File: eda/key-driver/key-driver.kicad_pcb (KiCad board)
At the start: 2 copper layers, 98.7 x 61.5 mm, 49 parts, among them J1 Conn_01x03_Socket, J10 Screw_Terminal_01x02, J11 Screw_Terminal_01x02, J12 Screw_Terminal_01x02, J13 Screw_Terminal_01x02, J14 Screw_Terminal_01x02, J15 Screw_Terminal_01x02, J2 Conn_01x03_Socket, J3 Screw_Terminal_01x02, J5 Screw_Terminal_01x02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

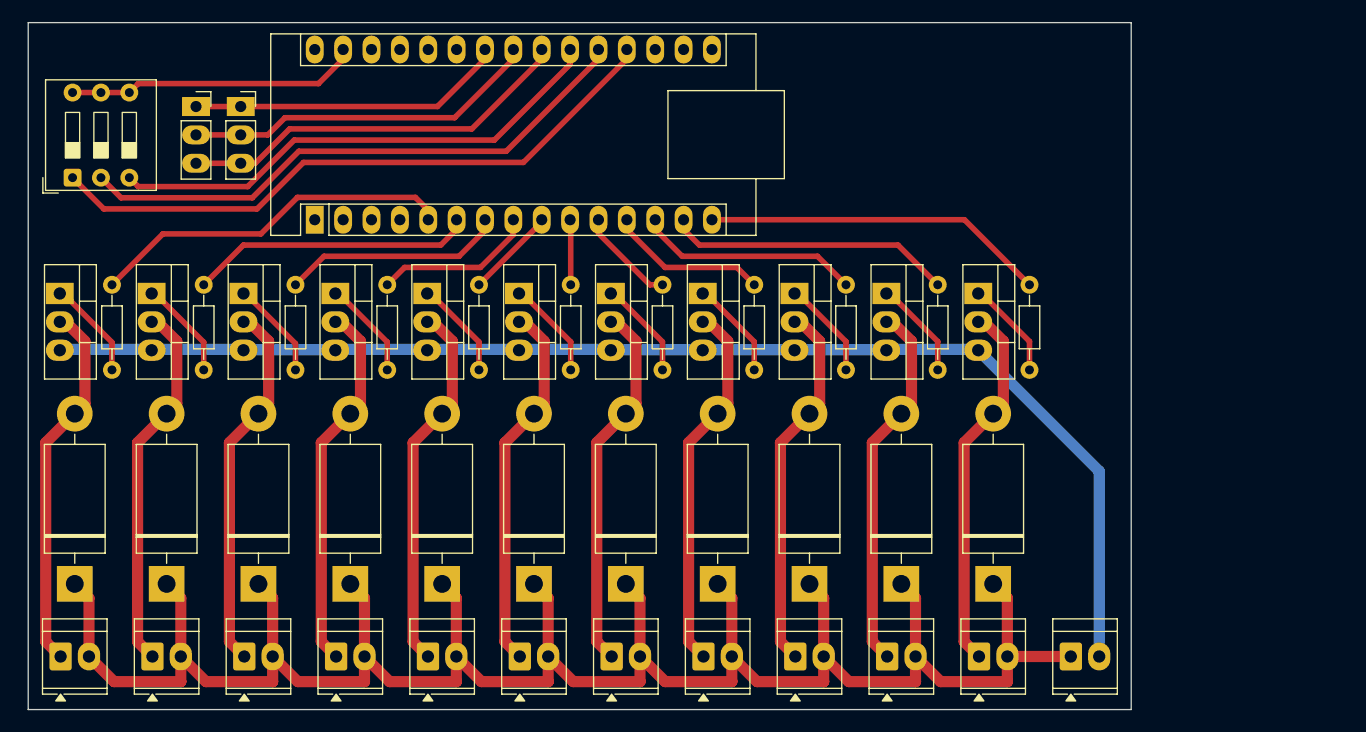
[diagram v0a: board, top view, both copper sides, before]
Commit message: Improve key driver circuit (r3)
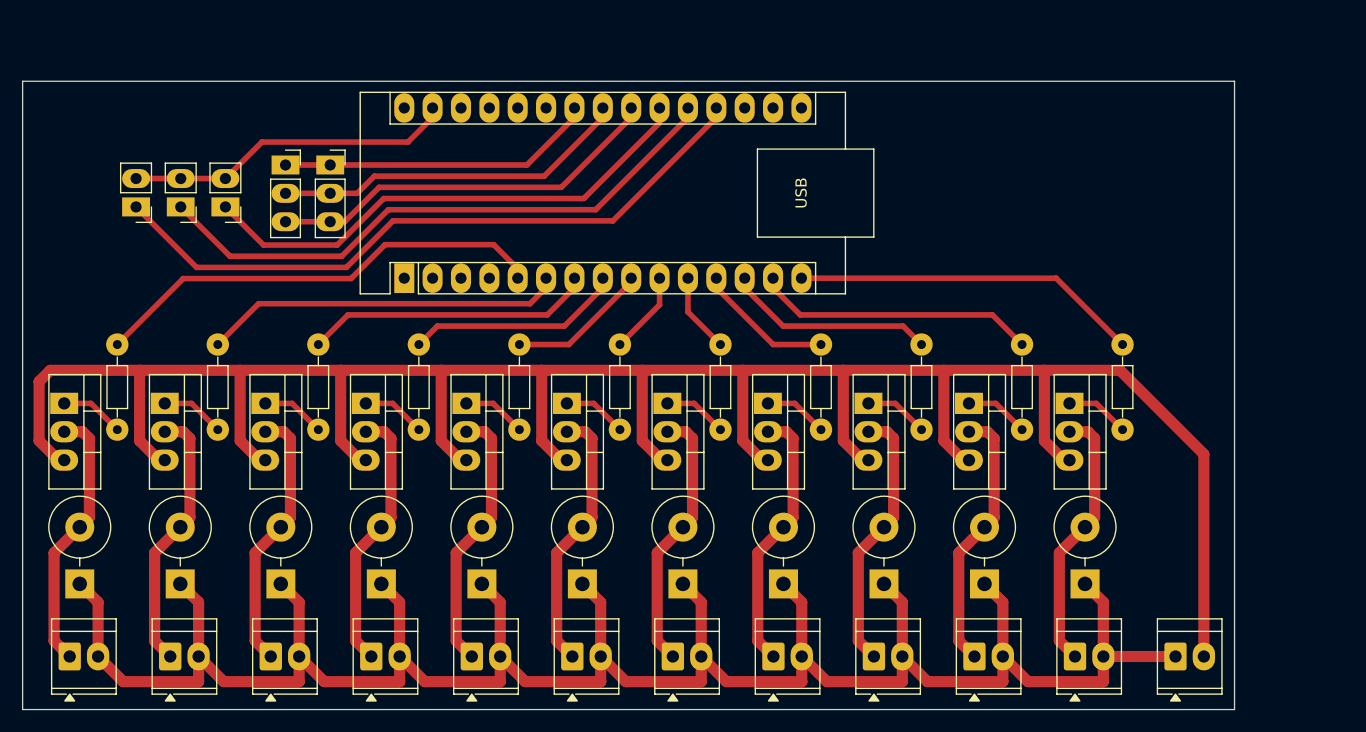
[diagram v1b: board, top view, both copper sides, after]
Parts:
- removed SW1: SW_DIP_x03, Button_Switch_THT:SW_DIP_SPSTx03_Slide_9.78x9.8mm_W7.62mm_P2.54mm
- added JP1: Jumper_2_Small_Open, self-playing-piano:PinHeader_1x02_P2.54mm_Vertical, F.Cu at (109.9, 80.9)
- added JP2: Jumper_2_Small_Open, self-playing-piano:PinHeader_1x02_P2.54mm_Vertical, F.Cu at (113.9, 80.9)
- added JP3: Jumper_2_Small_Open, self-playing-piano:PinHeader_1x02_P2.54mm_Vertical, F.Cu at (117.9, 80.9)
- D1, D10, D11, D2, D3, D4, D5, D6, D7, D8, D9: footprint Diode_THT:D_DO-201AD_P15.24mm_Horizontal -> Diode_THT:D_DO-201AE_P5.08mm_Vertical_KathodeUp
- moved Q11 12.8 mm to (193.5, 98.5)
- moved Q10 12.3 mm to (184.5, 98.5)
- moved Q9 11.9 mm to (175.5, 98.5)
- moved Q8 11.4 mm to (166.5, 98.5)
- moved Q7 11.1 mm to (157.5, 98.5)
- moved Q6 10.7 mm to (148.5, 98.5)
- moved Q5 10.4 mm to (139.5, 98.5)
- moved Q4 10.2 mm to (130.5, 98.5)
- moved Q3 10.0 mm to (121.5, 98.5)
- moved Q2 9.91 mm to (112.5, 98.5)
- moved R11 9.90 mm to (198.2, 93.2)
- moved Q1 9.85 mm to (103.5, 98.5)
- moved J1 9.57 mm to (127.3, 77.1)
- moved J2 9.57 mm to (123.3, 77.1)
- moved A1 9.57 mm to (133.9, 87.2)
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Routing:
- net GNDPWR: track 114.7 -> 227.0 mm
- net +24V: track 197.0 -> 207.3 mm
- net S06: track 33.2 -> 23.9 mm
- net S02: track 33.2 -> 23.9 mm
- net S10: track 33.2 -> 23.9 mm
- net S01: track 33.2 -> 23.9 mm
- net S00: track 33.2 -> 23.9 mm
- net S07: track 33.2 -> 23.9 mm
- net S05: track 33.2 -> 23.9 mm
- net S03: track 33.2 -> 23.9 mm
- net S08: track 33.2 -> 23.9 mm
- net S04: track 33.2 -> 23.9 mm
- net S09: track 33.2 -> 23.9 mm
- net G00: track 32.9 -> 41.3 mm
- net G01: track 25.5 -> 32.3 mm
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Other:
- board size 98.7 x 61.5 mm -> 108.5 x 56.2 mm

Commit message: Modify key driver schematic and PCB to use new key arrangement, JST connectors, and wider traces
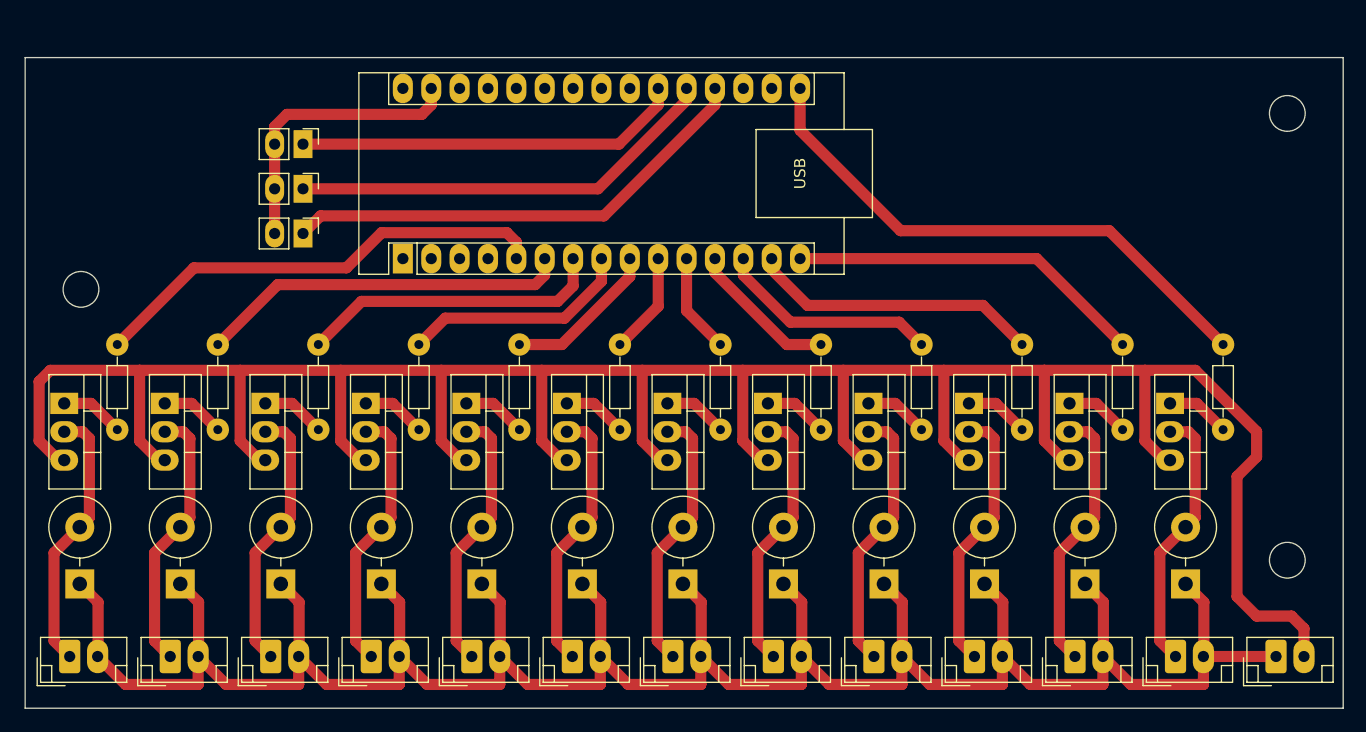
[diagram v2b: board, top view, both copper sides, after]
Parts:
- removed J14, J15: Screw_Terminal_01x02, self-playing-piano:TerminalBlock_TE_282834-2_1x02_P2.54mm_Horizontal
- added D12: SB2060, Diode_THT:D_DO-201AE_P5.08mm_Vertical_KathodeUp, F.Cu at (203.9, 114.6)
- added H1: MountingHole, MountingHole:MountingHole_3.2mm_M3, F.Cu at (105.0, 88.2)
- added H2: MountingHole, MountingHole:MountingHole_3.2mm_M3, F.Cu at (213.0, 72.5)
- added H3: MountingHole, MountingHole:MountingHole_3.2mm_M3, F.Cu at (213.0, 112.5)
- added J4: Screw_Terminal_01x02, self-playing-piano:JST_EH_B2B-EH-A_1x02_P2.50mm_Vertical, F.Cu at (122.0, 121.1)
- added Q12: IRLZ34N, self-playing-piano:TO-220-3_Vertical, F.Cu at (202.5, 98.5)
- added R12: 220, self-playing-piano:R_Axial_DIN0204_L3.6mm_D1.6mm_P7.62mm_Horizontal, F.Cu at (207.2, 93.2)
- J1, J2: value Conn_01x03_Socket -> Screw_Terminal_01x02; footprint self-playing-piano:PinSocket_1x03_P2.54mm_Vertical -> self-playing-piano:JST_EH_B2B-EH-A_1x02_P2.50mm_Vertical
- J10, J11, J12, J13, J3, J5, J6, J7, J8, J9: footprint self-playing-piano:TerminalBlock_TE_282834-2_1x02_P2.54mm_Horizontal -> self-playing-piano:JST_EH_B2B-EH-A_1x02_P2.50mm_Vertical
- moved J1 95.4 mm to (212.0, 121.1)
- moved J3 90.0 mm to (113.0, 121.1)
- moved J2 48.1 mm to (104.0, 121.1)
- moved J5 27.0 mm to (131.0, 121.1)
- moved J6 27.0 mm to (140.0, 121.1)
- moved J7 27.0 mm to (149.0, 121.1)
- moved J10 27.0 mm to (176.0, 121.1)
- moved J11 27.0 mm to (185.0, 121.1)
- moved J12 27.0 mm to (194.0, 121.1)
- moved J13 27.0 mm to (203.0, 121.1)
- moved J8 27.0 mm to (158.0, 121.1)
- moved J9 27.0 mm to (167.0, 121.1)
- moved JP1 15.1 mm to (124.9, 83.2), turned to -90 degrees
- moved JP2 11.1 mm to (124.9, 79.2), turned to -90 degrees
- moved JP3 8.94 mm to (124.9, 75.2), turned to -90 degrees
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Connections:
- A1 pad 16: unconnected-(A1-D13-Pad16) -> G11
- A1 pad 22: ~{LISTEN} -> unconnected-(A1-A3-Pad22)
- A1 pad 23: SDA -> unconnected-(A1-A4-Pad23)
- A1 pad 24: SCL -> unconnected-(A1-A5-Pad24)
- J1 pad 1: SCL -> +24V
- J1 pad 2: SDA -> GNDPWR
- J10 pad 1: S05 -> S08
- J11 pad 1: S06 -> S09
- J12 pad 1: S07 -> S10
- J13 pad 1: S08 -> S11
- J2 pad 1: SCL -> S00
- J2 pad 2: SDA -> +24V
- J3 pad 1: +24V -> S01
- J3 pad 2: GNDPWR -> +24V
- J5 pad 1: S00 -> S03
- J6 pad 1: S01 -> S04
- J7 pad 1: S02 -> S05
- J8 pad 1: S03 -> S06
- J9 pad 1: S04 -> S07
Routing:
- net G11: track 0.00 -> 49.6 mm
- net ~{LISTEN}: track 35.7 -> 0.00 mm
- net SDA: track 32.1 -> 0.00 mm
- net SCL: track 28.5 -> 0.00 mm
- net S11: track 0.00 -> 23.9 mm
- net +24V: track 207.3 -> 230.6 mm
- net GNDPWR: track 227.0 -> 247.2 mm
- net Net-(A1-A0): track 60.6 -> 43.1 mm
- net Net-(A1-A1): track 53.2 -> 38.7 mm
- net Net-(A1-A2): track 46.1 -> 34.7 mm
- net Net-(Q12-G): track 0.00 -> 5.72 mm
- net GNDD: track 29.7 -> 25.9 mm
- net G06: track 7.15 -> 8.95 mm
- net G05: track 7.41 -> 9.11 mm
- net G02: track 25.9 -> 27.4 mm
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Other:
- board size 108.5 x 56.2 mm -> 118 x 58.2 mm
